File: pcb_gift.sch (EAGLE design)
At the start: 19 parts, among them U1 ATTINY84, U2 BRM-2A18RA

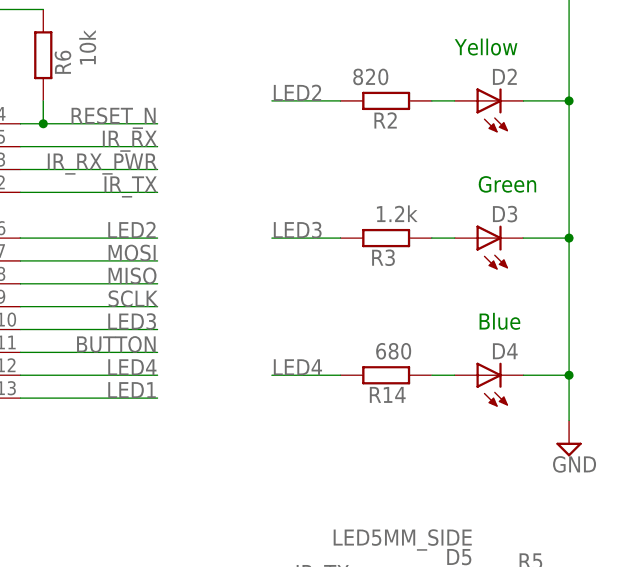
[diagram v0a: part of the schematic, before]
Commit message: updated code for new revision and cleaned things up
- added bom
- updated firmware for this version
- firmware has deeper sleep mode
- added scripts to compile/upload to board
- added .gitignore
- updated readme
- added images of the final board schematic, and component locations
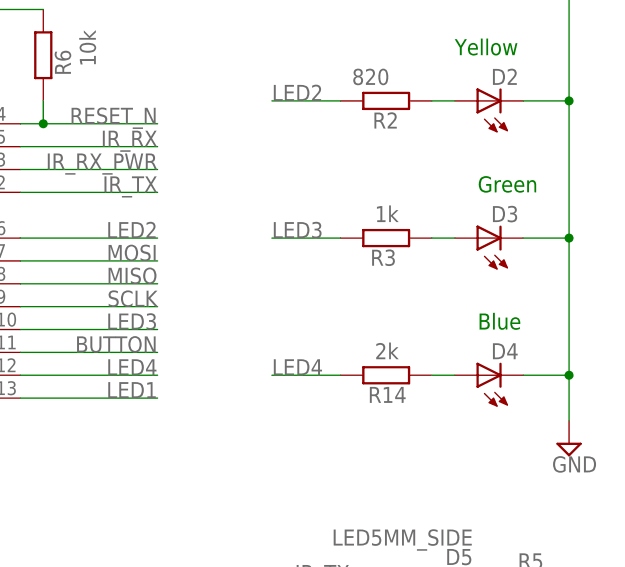
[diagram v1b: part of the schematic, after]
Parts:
- R14: value 680 -> 2k
- R3: value 1.2k -> 1k
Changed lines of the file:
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@@
 <part name="R1" library="resistor" deviceset="R-EU_" device="R0805" value="560"/>
 <part name="R2" library="resistor" deviceset="R-EU_" device="R0805" value="820"/>
-<part name="R3" library="resistor" deviceset="R-EU_" device="R0805" value="1.2k"/>
-<part name="R14" library="resistor" deviceset="R-EU_" device="R0805" value="680"/>
+<part name="R3" library="resistor" deviceset="R-EU_" device="R0805" value="1k"/>
+<part name="R14" library="resistor" deviceset="R-EU_" device="R0805" value="2k"/>
 <part name="D5" library="widget" deviceset="LED5MM_SIDE" device=""/>
 <part name="R5" library="resistor" deviceset="R-EU_" device="R0805" value="560"/>
